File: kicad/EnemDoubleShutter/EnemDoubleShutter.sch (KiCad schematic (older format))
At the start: 7 parts, among them J1 Conn_01x02, J2 Bouton 1, J3 Bouton 2, U1 NodeMCU_Amica_R2

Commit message: Corrections et finalisation PCB
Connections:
- net +3V3: no longer U1.11 (3V3), U1.16 (3V3)
- net GND: no longer U1.10 (GND)
- net at U1.20 (D8): now also J3.3 (Pin_3)
- net at U1.21 (D7): now also J3.2 (Pin_2); no longer Relay2.5 (IN2)
- net at U1.22 (D6): now also Relay2.5 (IN2); no longer Relay2.4 (IN1)
- net at U1.23 (D5): now also Relay2.4 (IN1)
- net at U1.4 (SD3): no longer J3.3 (Pin_3)
- net at U1.5 (SD2): no longer J3.2 (Pin_2)
- no-connect marks 30 -> 33
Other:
- moved on the sheet: J3
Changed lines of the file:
@@
 LIBS:contrib
 LIBS:valves
+LIBS:enem
 LIBS:nodemcu
-LIBS:enem
 LIBS:EnemDoubleShutter-cache
 EELAYER 25 0
@@
 $EndDescr
 $Comp
-L GND #PWR01
-U 1 1 5AE0C572
-P 4650 4750
-F 0 "#PWR01" H 4650 4500 50  0001 C CNN
-F 1 "GND" H 4650 4600 50  0000 C CNN
-F 2 "" H 4650 4750 50  0001 C CNN
-F 3 "" H 4650 4750 50  0001 C CNN
-	1    4650 4750
-	-1   0    0    1
-$EndComp
-$Comp
-L +5V #PWR02
+L +5V #PWR01
 U 1 1 5AE34FA2
 P 4650 4850
-F 0 "#PWR02" H 4650 4700 50  0001 C CNN
+F 0 "#PWR01" H 4650 4700 50  0001 C CNN
 F 1 "+5V" H 4650 4990 50  0000 C CNN
 F 2 "" H 4650 4850 50  0001 C CNN
@@
 NoConn ~ 5800 4650
 $Comp
-L PWR_FLAG #FLG03
+L PWR_FLAG #FLG02
 U 1 1 5AE354EB
 P 2600 2750
-F 0 "#FLG03" H 2600 2825 50  0001 C CNN
+F 0 "#FLG02" H 2600 2825 50  0001 C CNN
 F 1 "PWR_FLAG" H 2600 2900 50  0000 C CNN
 F 2 "" H 2600 2750 50  0001 C CNN
@@
 $EndComp
 $Comp
-L PWR_FLAG #FLG04
+L PWR_FLAG #FLG03
 U 1 1 5AE35505
 P 3050 2750
-F 0 "#FLG04" H 3050 2825 50  0001 C CNN
+F 0 "#FLG03" H 3050 2825 50  0001 C CNN
 F 1 "PWR_FLAG" H 3050 2900 50  0000 C CNN
 F 2 "" H 3050 2750 50  0001 C CNN
@@
 $EndComp
 $Comp
-L GND #PWR05
+L GND #PWR04
 U 1 1 5AE3551F
 P 2600 2750
-F 0 "#PWR05" H 2600 2500 50  0001 C CNN
+F 0 "#PWR04" H 2600 2500 50  0001 C CNN
 F 1 "GND" H 2600 2600 50  0000 C CNN
 F 2 "" H 2600 2750 50  0001 C CNN
@@
 $EndComp
 $Comp
-L +5V #PWR06
+L +5V #PWR05
 U 1 1 5AE35537
 P 3050 2750
-F 0 "#PWR06" H 3050 2600 50  0001 C CNN
+F 0 "#PWR05" H 3050 2600 50  0001 C CNN
 F 1 "+5V" H 3050 2890 50  0000 C CNN
 F 2 "" H 3050 2750 50  0001 C CNN
@@
 $EndComp
 $Comp
-L GND #PWR07
+L GND #PWR06
 U 1 1 5AE62183
 P 3750 3450
-F 0 "#PWR07" H 3750 3200 50  0001 C CNN
+F 0 "#PWR06" H 3750 3200 50  0001 C CNN
 F 1 "GND" H 3750 3300 50  0000 C CNN
 F 2 "" H 3750 3450 50  0001 C CNN
@@
 $EndComp
 $Comp
-L +5V #PWR08
+L +5V #PWR07
 U 1 1 5AE6219F
 P 3750 3350
-F 0 "#PWR08" H 3750 3200 50  0001 C CNN
+F 0 "#PWR07" H 3750 3200 50  0001 C CNN
 F 1 "+5V" H 3750 3490 50  0000 C CNN
 F 2 "" H 3750 3350 50  0001 C CNN
@@
 $EndComp
 $Comp
-L GND #PWR09
+L GND #PWR08
 U 1 1 5AE629DE
 P 6000 2500
-F 0 "#PWR09" H 6000 2250 50  0001 C CNN
+F 0 "#PWR08" H 6000 2250 50  0001 C CNN
 F 1 "GND" H 6000 2350 50  0000 C CNN
 F 2 "" H 6000 2500 50  0001 C CNN
@@
 $EndComp
 $Comp
-L +3.3V #PWR010
-U 1 1 5AE62AB6
-P 5950 4850
-F 0 "#PWR010" H 5950 4700 50  0001 C CNN
-F 1 "+3.3V" H 5950 4990 50  0000 C CNN
-F 2 "" H 5950 4850 50  0001 C CNN
-F 3 "" H 5950 4850 50  0001 C CNN
-	1    5950 4850
-	-1   0    0    1
-$EndComp
-$Comp
-L +3.3V #PWR011
+L +3.3V #PWR09
 U 1 1 5AE62AFA
 P 3500 2750
-F 0 "#PWR011" H 3500 2600 50  0001 C CNN
+F 0 "#PWR09" H 3500 2600 50  0001 C CNN
 F 1 "+3.3V" H 3500 2890 50  0000 C CNN
 F 2 "" H 3500 2750 50  0001 C CNN
@@
 $EndComp
 $Comp
-L PWR_FLAG #FLG012
+L PWR_FLAG #FLG010
 U 1 1 5AE62B41
 P 3500 2750
-F 0 "#FLG012" H 3500 2825 50  0001 C CNN
+F 0 "#FLG010" H 3500 2825 50  0001 C CNN
 F 1 "PWR_FLAG" H 3500 2900 50  0000 C CNN
 F 2 "" H 3500 2750 50  0001 C CNN
@@
 $EndComp
 $Comp
-L +3.3V #PWR013
+L +3.3V #PWR011
 U 1 1 5AE62B99
 P 5800 2600
-F 0 "#PWR013" H 5800 2450 50  0001 C CNN
+F 0 "#PWR011" H 5800 2450 50  0001 C CNN
 F 1 "+3.3V" H 5800 2740 50  0000 C CNN
 F 2 "" H 5800 2600 50  0001 C CNN
@@
 $EndComp
 $Comp
-L +5V #PWR014
+L +5V #PWR012
 U 1 1 5AE62BE5
 P 5550 2700
-F 0 "#PWR014" H 5550 2550 50  0001 C CNN
+F 0 "#PWR012" H 5550 2550 50  0001 C CNN
 F 1 "+5V" H 5550 2840 50  0000 C CNN
 F 2 "" H 5550 2700 50  0001 C CNN
@@
 $EndComp
 $Comp
-L GND #PWR015
+L GND #PWR013
 U 1 1 5AE6306B
 P 6350 3650
-F 0 "#PWR015" H 6350 3400 50  0001 C CNN
+F 0 "#PWR013" H 6350 3400 50  0001 C CNN
 F 1 "GND" H 6350 3500 50  0000 C CNN
 F 2 "" H 6350 3650 50  0001 C CNN
@@
 $EndComp
 $Comp
-L GND #PWR016
+L GND #PWR014
 U 1 1 5AE8BBDB
 P 7400 3750
-F 0 "#PWR016" H 7400 3500 50  0001 C CNN
+F 0 "#PWR014" H 7400 3500 50  0001 C CNN
 F 1 "GND" H 7400 3600 50  0000 C CNN
 F 2 "" H 7400 3750 50  0001 C CNN
@@
 $EndComp
 $Comp
-L +3.3V #PWR017
+L +3.3V #PWR015
 U 1 1 5AE8BBF8
 P 7200 3850
-F 0 "#PWR017" H 7200 3700 50  0001 C CNN
+F 0 "#PWR015" H 7200 3700 50  0001 C CNN
 F 1 "+3.3V" H 7200 3990 50  0000 C CNN
 F 2 "" H 7200 3850 50  0001 C CNN
@@
 $EndComp
 $Comp
-L +5V #PWR018
+L +5V #PWR016
 U 1 1 5AE8BC15
 P 7000 3950
-F 0 "#PWR018" H 7000 3800 50  0001 C CNN
+F 0 "#PWR016" H 7000 3800 50  0001 C CNN
 F 1 "+5V" H 7000 4090 50  0000 C CNN
 F 2 "" H 7000 3950 50  0001 C CNN
@@
 L Conn_01x03 J3
 U 1 1 5AE8C308
-P 4300 3850
-F 0 "J3" H 4300 4050 50  0000 C CNN
-F 1 "Bouton 2" H 4300 3650 50  0000 C CNN
-F 2 "enemLib:Bornier3" H 4300 3850 50  0001 C CNN
-F 3 "" H 4300 3850 50  0001 C CNN
-	1    4300 3850
-	-1   0    0    -1
-$EndComp
-$Comp
-L GND #PWR019
+P 7200 4600
+F 0 "J3" H 7200 4800 50  0000 C CNN
+F 1 "Bouton 2" H 7200 4400 50  0000 C CNN
+F 2 "enemLib:Bornier3" H 7200 4600 50  0001 C CNN
+F 3 "" H 7200 4600 50  0001 C CNN
+	1    7200 4600
+	1    0    0    -1
+$EndComp
+$Comp
+L GND #PWR017
 U 1 1 5AE8C3D5
-P 4600 3750
-F 0 "#PWR019" H 4600 3500 50  0001 C CNN
-F 1 "GND" H 4600 3600 50  0000 C CNN
-F 2 "" H 4600 3750 50  0001 C CNN
-F 3 "" H 4600 3750 50  0001 C CNN
-	1    4600 3750
-	1    0    0    1
-$EndComp
-NoConn ~ 5800 4150
+P 6900 4500
+F 0 "#PWR017" H 6900 4250 50  0001 C CNN
+F 1 "GND" H 6900 4350 50  0000 C CNN
+F 2 "" H 6900 4500 50  0001 C CNN
+F 3 "" H 6900 4500 50  0001 C CNN
+	1    6900 4500
+	-1   0    0    1
+$EndComp
 $Comp
 L NodeMCU_Amica_R2 U1
@@
 $EndComp
 NoConn ~ 4900 3950
-NoConn ~ 5800 4450
-$Comp
-L +3.3V #PWR020
-U 1 1 5AE8D74B
-P 4400 4450
-F 0 "#PWR020" H 4400 4300 50  0001 C CNN
-F 1 "+3.3V" H 4400 4590 50  0000 C CNN
-F 2 "" H 4400 4450 50  0001 C CNN
-F 3 "" H 4400 4450 50  0001 C CNN
-	1    4400 4450
-	-1   0    0    1
-$EndComp
-$Comp
-L GND #PWR021
-U 1 1 5AE8D72B
-P 4650 4350
-F 0 "#PWR021" H 4650 4100 50  0001 C CNN
-F 1 "GND" H 4650 4200 50  0000 C CNN
-F 2 "" H 4650 4350 50  0001 C CNN
-F 3 "" H 4650 4350 50  0001 C CNN
-	1    4650 4350
-	-1   0    0    1
-$EndComp
-Wire Wire Line
-	4650 4750 4900 4750
 Wire Wire Line
 	2550 3350 2650 3350
@@
 	4900 4850 4650 4850
 Wire Wire Line
-	5800 4850 5950 4850
-Wire Wire Line
 	6000 2500 6150 2500
 Wire Wire Line
@@
 	6000 3650 5800 3650
 Wire Wire Line
-	7550 4250 5800 4250
-Wire Wire Line
-	5800 4350 7550 4350
-Wire Wire Line
-	4600 3750 4500 3750
-Wire Wire Line
-	4500 3850 4900 3850
-Wire Wire Line
-	4500 3950 4750 3950
-Wire Wire Line
-	4750 3950 4750 3750
-Wire Wire Line
-	4750 3750 4900 3750
-Wire Wire Line
-	4900 4350 4650 4350
-Wire Wire Line
-	4900 4450 4400 4450
-$Comp
-L GND #PWR022
+	6900 4500 7000 4500
+$Comp
+L GND #PWR018
 U 1 1 5AE8D865
-P 5900 4100
-F 0 "#PWR022" H 5900 3850 50  0001 C CNN
-F 1 "GND" H 5900 3950 50  0000 C CNN
-F 2 "" H 5900 4100 50  0001 C CNN
-F 3 "" H 5900 4100 50  0001 C CNN
-	1    5900 4100
+P 5950 4050
+F 0 "#PWR018" H 5950 3800 50  0001 C CNN
+F 1 "GND" H 5950 3900 50  0000 C CNN
+F 2 "" H 5950 4050 50  0001 C CNN
+F 3 "" H 5950 4050 50  0001 C CNN
+	1    5950 4050
 	0    -1   -1   0
 $EndComp
 $Comp
-L +3.3V #PWR023
+L +3.3V #PWR019
 U 1 1 5AE8D885
 P 6250 3950
-F 0 "#PWR023" H 6250 3800 50  0001 C CNN
+F 0 "#PWR019" H 6250 3800 50  0001 C CNN
 F 1 "+3.3V" H 6250 4090 50  0000 C CNN
 F 2 "" H 6250 3950 50  0001 C CNN
 F 3 "" H 6250 3950 50  0001 C CNN
 	1    6250 3950
-	-1   0    0    1
-$EndComp
-$Comp
-L GND #PWR024
+	0    1    1    0
+$EndComp
+$Comp
+L GND #PWR020
 U 1 1 5AE8D8A5
 P 6000 4750
-F 0 "#PWR024" H 6000 4500 50  0001 C CNN
+F 0 "#PWR020" H 6000 4500 50  0001 C CNN
 F 1 "GND" H 6000 4600 50  0000 C CNN
 F 2 "" H 6000 4750 50  0001 C CNN
@@
 $EndComp
 Wire Wire Line
-	5800 4050 5900 4050
-Wire Wire Line
-	5900 4050 5900 4100
-Wire Wire Line
 	5800 3950 6250 3950
 Wire Wire Line
@@
 NoConn ~ 7550 4450
 NoConn ~ 7550 4550
+NoConn ~ 4900 3750
+NoConn ~ 4900 3850
+Wire Wire Line
+	5800 4050 5950 4050
+Wire Wire Line
+	5800 4150 7550 4150
+Wire Wire Line
+	7550 4150 7550 4250
+Wire Wire Line
+	5800 4250 7500 4250
+Wire Wire Line
+	7500 4250 7500 4350
+Wire Wire Line
+	7500 4350 7550 4350
+Wire Wire Line
+	5800 4350 6700 4350
+Wire Wire Line
+	6700 4350 6700 4600
+Wire Wire Line
+	6700 4600 7000 4600
+Wire Wire Line
+	5800 4450 6600 4450
+Wire Wire Line
+	6600 4450 6600 4700
+Wire Wire Line
+	6600 4700 7000 4700
+NoConn ~ 4900 4350
+NoConn ~ 4900 4450
+$Comp
+L GND #PWR021
+U 1 1 5AEF0CFA
+P 4800 4750
+F 0 "#PWR021" H 4800 4500 50  0001 C CNN
+F 1 "GND" H 4800 4600 50  0000 C CNN
+F 2 "" H 4800 4750 50  0001 C CNN
+F 3 "" H 4800 4750 50  0001 C CNN
+	1    4800 4750
+	0    1    1    0
+$EndComp
+Wire Wire Line
+	4800 4750 4900 4750
+NoConn ~ 5800 4850
 $EndSCHEMATC

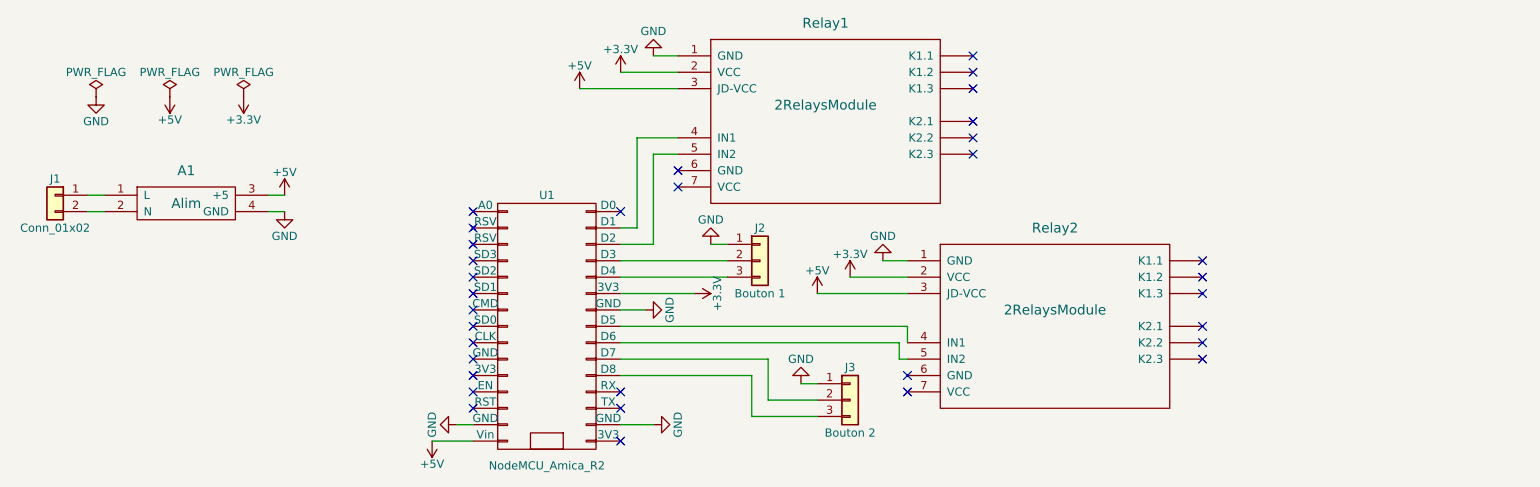
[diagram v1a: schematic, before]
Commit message: Ajout doc sur schéma + connection volets
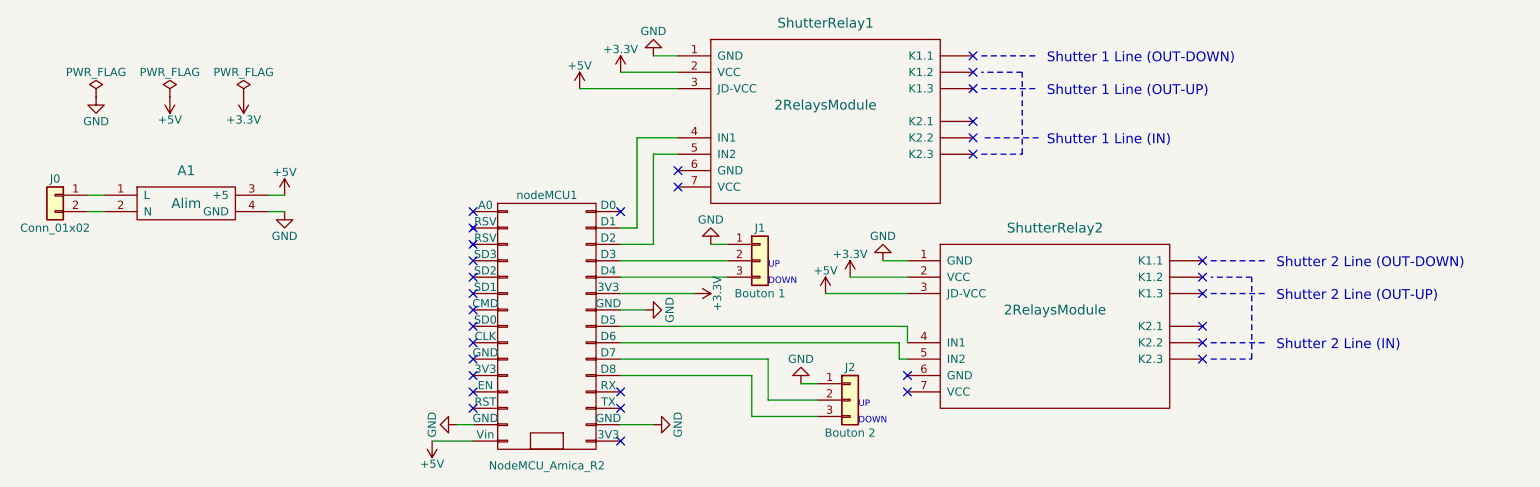
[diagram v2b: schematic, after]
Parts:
- renumbered J1 to J0, J2 to J1, J3 to J2, Relay1 to ShutterRelay1, Relay2 to ShutterRelay2, U1 to nodeMCU1
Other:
- note added: "DOWN"
- note added: "Shutter 1 Line (IN)"
- note added: "Shutter 1 Line (OUT-DOWN)"
- note added: "Shutter 1 Line (OUT-UP)"
- note added: "Shutter 2 Line (IN)"
- note added: "Shutter 2 Line (OUT-DOWN)"
- note added: "Shutter 2 Line (OUT-UP)"
- note added: "UP"
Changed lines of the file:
@@
 $EndComp
 $Comp
-L Conn_01x02 J1
+L Conn_01x02 J0
 U 1 1 5AE61E8A
 P 2350 3350
-F 0 "J1" H 2350 3450 50  0000 C CNN
+F 0 "J0" H 2350 3450 50  0000 C CNN
 F 1 "Conn_01x02" H 2350 3150 50  0000 C CNN
 F 2 "enemLib:Bornier2" H 2350 3350 50  0001 C CNN
@@
 $EndComp
 $Comp
-L 2RelaysModule Relay1
+L 2RelaysModule ShutterRelay1
 U 1 1 5AE6251D
 P 7050 2800
-F 0 "Relay1" H 7050 3300 60  0000 C CNN
+F 0 "ShutterRelay1" H 7050 3300 60  0000 C CNN
 F 1 "2RelaysModule" H 7050 2800 60  0000 C CNN
 F 2 "enemLib:relayModule" H 7050 3300 60  0001 C CNN
@@
 NoConn ~ 7950 3100
 $Comp
-L Conn_01x03 J2
+L Conn_01x03 J1
 U 1 1 5AE62F81
 P 6650 3750
-F 0 "J2" H 6650 3950 50  0000 C CNN
+F 0 "J1" H 6650 3950 50  0000 C CNN
 F 1 "Bouton 1" H 6650 3550 50  0000 C CNN
 F 2 "enemLib:Bornier3" H 6650 3750 50  0001 C CNN
@@
 $EndComp
 $Comp
-L 2RelaysModule Relay2
+L 2RelaysModule ShutterRelay2
 U 1 1 5AE8BB79
 P 8450 4050
-F 0 "Relay2" H 8450 4550 60  0000 C CNN
+F 0 "ShutterRelay2" H 8450 4550 60  0000 C CNN
 F 1 "2RelaysModule" H 8450 4050 60  0000 C CNN
 F 2 "enemLib:relayModule" H 8450 4550 60  0001 C CNN
@@
 L +5V #PWR016
 U 1 1 5AE8BC15
-P 7000 3950
-F 0 "#PWR016" H 7000 3800 50  0001 C CNN
-F 1 "+5V" H 7000 4090 50  0000 C CNN
-F 2 "" H 7000 3950 50  0001 C CNN
-F 3 "" H 7000 3950 50  0001 C CNN
-	1    7000 3950
+P 7050 3950
+F 0 "#PWR016" H 7050 3800 50  0001 C CNN
+F 1 "+5V" H 7050 4090 50  0000 C CNN
+F 2 "" H 7050 3950 50  0001 C CNN
+F 3 "" H 7050 3950 50  0001 C CNN
+	1    7050 3950
 	1    0    0    -1
 $EndComp
@@
 NoConn ~ 9350 4350
 $Comp
-L Conn_01x03 J3
+L Conn_01x03 J2
 U 1 1 5AE8C308
 P 7200 4600
-F 0 "J3" H 7200 4800 50  0000 C CNN
+F 0 "J2" H 7200 4800 50  0000 C CNN
 F 1 "Bouton 2" H 7200 4400 50  0000 C CNN
 F 2 "enemLib:Bornier3" H 7200 4600 50  0001 C CNN
@@
 $EndComp
 $Comp
-L NodeMCU_Amica_R2 U1
+L NodeMCU_Amica_R2 nodeMCU1
 U 1 1 5AE34C07
 P 5350 4150
-F 0 "U1" H 5350 4950 50  0000 C CNN
+F 0 "nodeMCU1" H 5350 4950 50  0000 C CNN
 F 1 "NodeMCU_Amica_R2" H 5350 3300 50  0000 C CNN
 F 2 "enemLib:NodeMCU_simple" H 5600 4150 50  0001 C CNN
@@
 	7200 3850 7550 3850
 Wire Wire Line
-	7000 3950 7550 3950
+	7050 3950 7550 3950
 Wire Wire Line
 	5900 3000 5900 3550
@@
 	4800 4750 4900 4750
 NoConn ~ 5800 4850
+Wire Notes Line
+	8350 3000 8000 3000
+Wire Notes Line
+	8000 3100 8250 3100
+Wire Notes Line
+	8250 3100 8250 2600
+Wire Notes Line
+	8250 2600 8000 2600
+Wire Notes Line
+	8000 2700 8350 2700
+Wire Notes Line
+	8000 2500 8350 2500
+Text Notes 8400 2550 0    60   ~ 0
+Shutter 1 Line (OUT-DOWN)
+Text Notes 8400 2750 0    60   ~ 0
+Shutter 1 Line (OUT-UP)
+Wire Notes Line
+	9400 4250 9750 4250
+Wire Notes Line
+	9400 4350 9650 4350
+Wire Notes Line
+	9650 4350 9650 3850
+Wire Notes Line
+	9650 3850 9400 3850
+Wire Notes Line
+	9400 3950 9750 3950
+Wire Notes Line
+	9400 3750 9750 3750
+Text Notes 8400 3050 0    60   ~ 0
+Shutter 1 Line (IN)
+Text Notes 7250 4650 0    39   ~ 0
+UP
+Text Notes 7250 4750 0    39   ~ 0
+DOWN
+Text Notes 6700 3800 0    39   ~ 0
+UP
+Text Notes 6700 3900 0    39   ~ 0
+DOWN
+Text Notes 9800 4300 0    60   ~ 0
+Shutter 2 Line (IN)
+Text Notes 9800 4000 0    60   ~ 0
+Shutter 2 Line (OUT-UP)
+Text Notes 9800 3800 0    60   ~ 0
+Shutter 2 Line (OUT-DOWN)
 $EndSCHEMATC
